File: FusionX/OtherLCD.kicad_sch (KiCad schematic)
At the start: 1 part, among them J3 OtherLCD

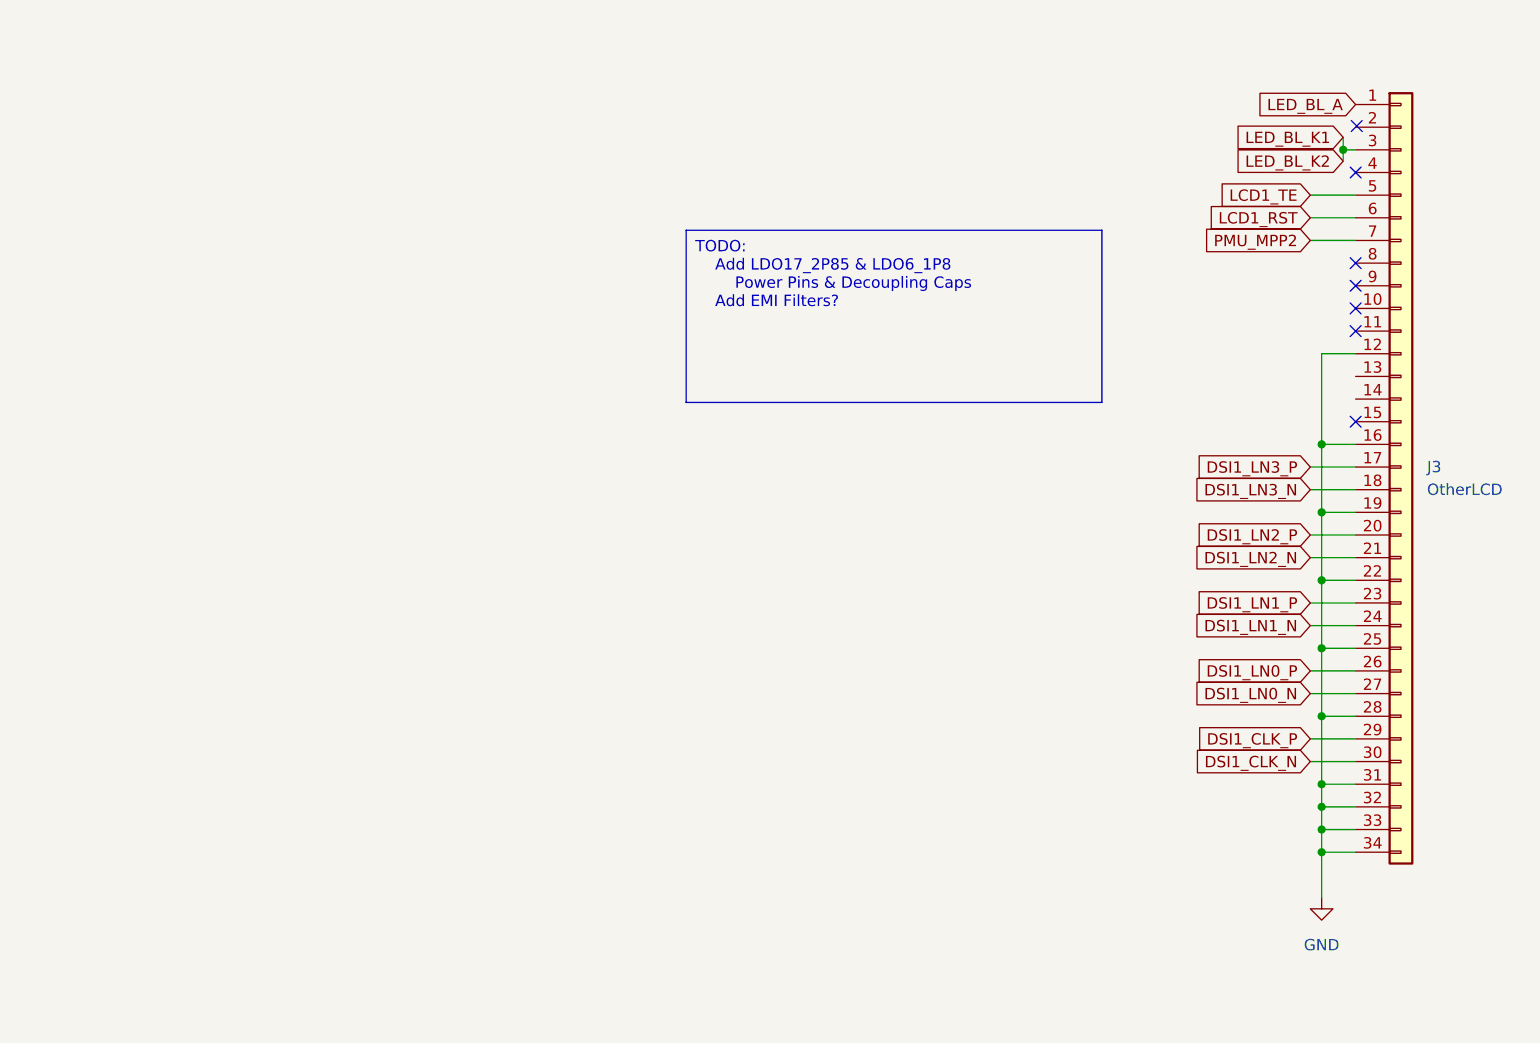
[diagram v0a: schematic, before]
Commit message: Implemented: 	USB-C Super Speed 	Capacitve Touch Screen 	Secondary LCD
Started On:
	PCB Layout
	Case Design
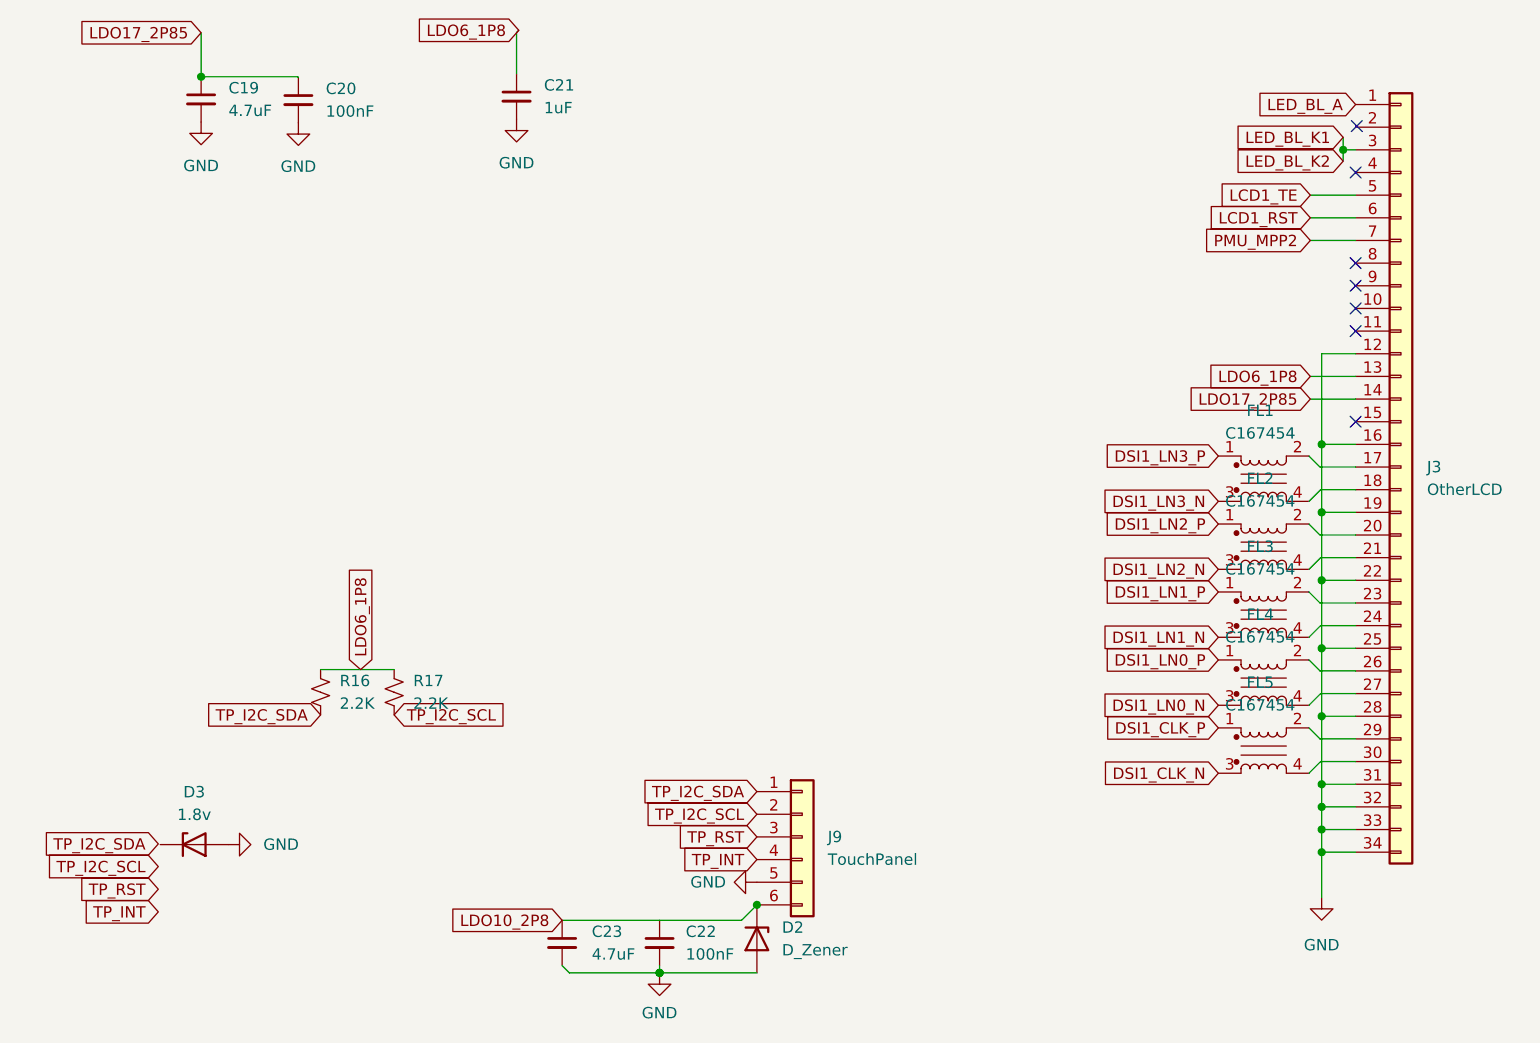
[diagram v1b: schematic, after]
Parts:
- added C19, C23: 4.7uF, symbol Device:C_Small
- added C20, C22: 100nF, symbol Device:C_Small
- added C21: 1uF, symbol Device:C_Small
- added D2: D_Zener, symbol Device:D_Zener
- added D3: 1.8v, symbol Device:D_Zener
- added FL1, FL2, FL3, FL4, FL5: C167454, Phone:DLP0SN900HL2L, symbol Device:Filter_EMI_CommonMode
- added J9: TouchPanel, symbol Connector_Generic:Conn_01x06
- added R16, R17: 2.2K, symbol Device:R_Small_US
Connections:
- net DSI1_CLK_N: now also FL5.3; no longer J3.30 (Pin_30)
- net DSI1_CLK_P: now also FL5.1; no longer J3.29 (Pin_29)
- net DSI1_LN0_N: now also FL4.3; no longer J3.27 (Pin_27)
- net DSI1_LN0_P: now also FL4.1; no longer J3.26 (Pin_26)
- net DSI1_LN1_N: now also FL3.3; no longer J3.24 (Pin_24)
- net DSI1_LN1_P: now also FL3.1; no longer J3.23 (Pin_23)
- net DSI1_LN2_N: now also FL2.3; no longer J3.21 (Pin_21)
- net DSI1_LN2_P: now also FL2.1; no longer J3.20 (Pin_20)
- net DSI1_LN3_N: now also FL1.3; no longer J3.18 (Pin_18)
- net DSI1_LN3_P: now also FL1.1; no longer J3.17 (Pin_17)
- net GND: now also C19.2, C20.2, C21.2, C22.2, C23.2, D2.2 (A), D3.2 (A), J9.5 (Pin_5)
- net LDO6_1P8: now reaches J3.13 (Pin_13)
- net LDO6_1P8: now also C21.1, R16.1, R17.1
- net LDO17_2P85: now reaches J3.14 (Pin_14)
- net LDO17_2P85: now also C19.1, C20.1
- new net: FL3.2, J3.23 (Pin_23)
- new net: FL3.4, J3.24 (Pin_24)
- new net: FL1.2, J3.17 (Pin_17)
- new net: FL1.4, J3.18 (Pin_18)
- new net: FL2.2, J3.20 (Pin_20)
- new net: FL2.4, J3.21 (Pin_21)
- new net: FL4.2, J3.26 (Pin_26)
- new net: FL4.4, J3.27 (Pin_27)
- new net: FL5.2, J3.29 (Pin_29)
- new net: FL5.4, J3.30 (Pin_30)
- new net LDO10_2P8: C23.1, D2.1 (K), J9.6 (Pin_6)
- new net TP_I2C_SCL: J9.2 (Pin_2), R17.2
- new net TP_I2C_SDA: J9.1 (Pin_1), R16.2
- new net TP_INT: J9.4 (Pin_4)
- new net TP_RST: J9.3 (Pin_3)
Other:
- company: (none) -> NoahGWood
- title: (none) -> FusionX

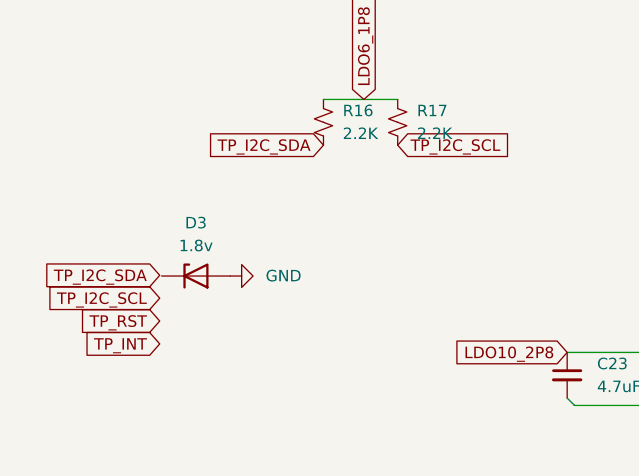
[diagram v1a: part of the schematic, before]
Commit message: Removed unneeded files
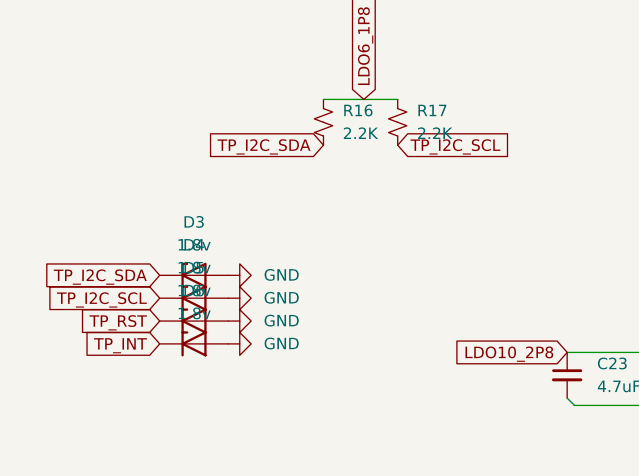
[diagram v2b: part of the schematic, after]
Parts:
- added D4, D5, D6: 1.8v, symbol Device:D_Zener
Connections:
- net GND: now also D4.2 (A), D5.2 (A), D6.2 (A)
- net TP_I2C_SCL: now also D4.1 (K)
- net TP_I2C_SDA: now also D3.1 (K)
- net TP_INT: now also D6.1 (K)
- net TP_RST: now also D5.1 (K)
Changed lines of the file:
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@@
+    )
+  )
+  (symbol (lib_id "Device:D_Zener") (at 40.5211 133.4371 0) (unit 1)
+    (in_bom yes) (on_board yes) (dnp no) (fields_autoplaced)
+    (property "Reference" "D4" (at 40.5211 127.5506 0)
+      (effects (font (size 1.27 1.27)))
+    )
+    (property "Value" "1.8v" (at 40.5211 130.0906 0)
+      (effects (font (size 1.27 1.27)))
+    )
+    (property "Footprint" "" (at 40.5211 133.4371 0)
+      (effects (font (size 1.27 1.27)) hide)
+    )
+    (property "Datasheet" "~" (at 40.5211 133.4371 0)
+      (effects (font (size 1.27 1.27)) hide)
+    )
+    (pin "1")
+    (pin "2")
+    (instances
+      (project "FusionX"
+        (path "/91d1c248-6dd5-47d7-a0ee-1ed6541bbbfb/cc596c66-0287-4740-9ece-2b1e4f18f9fd"
+          (reference "D4") (unit 1)
+        )
+      )
     )
   )
@@
     )
   )
-  (symbol (lib_id "Device:D_Zener") (at 40.7344 130.9745 0) (unit 1)
-    (in_bom yes) (on_board yes) (dnp no) (fields_autoplaced)
-    (property "Reference" "D3" (at 40.7344 125.088 0)
-      (effects (font (size 1.27 1.27)))
-    )
-    (property "Value" "1.8v" (at 40.7344 127.628 0)
-      (effects (font (size 1.27 1.27)))
-    )
-    (property "Footprint" "" (at 40.7344 130.9745 0)
-      (effects (font (size 1.27 1.27)) hide)
-    )
-    (property "Datasheet" "~" (at 40.7344 130.9745 0)
+  (symbol (lib_id "Device:D_Zener") (at 40.5211 138.5171 0) (unit 1)
+    (in_bom yes) (on_board yes) (dnp no) (fields_autoplaced)
+    (property "Reference" "D6" (at 40.5211 132.6306 0)
+      (effects (font (size 1.27 1.27)))
+    )
+    (property "Value" "1.8v" (at 40.5211 135.1706 0)
+      (effects (font (size 1.27 1.27)))
+    )
+    (property "Footprint" "" (at 40.5211 138.5171 0)
+      (effects (font (size 1.27 1.27)) hide)
+    )
+    (property "Datasheet" "~" (at 40.5211 138.5171 0)
+      (effects (font (size 1.27 1.27)) hide)
+    )
+    (pin "1")
+    (pin "2")
+    (instances
+      (project "FusionX"
+        (path "/91d1c248-6dd5-47d7-a0ee-1ed6541bbbfb/cc596c66-0287-4740-9ece-2b1e4f18f9fd"
+          (reference "D6") (unit 1)
+        )
+      )
+    )
+  )
+  (symbol (lib_id "Device:D_Zener") (at 40.5211 130.8971 0) (unit 1)
+    (in_bom yes) (on_board yes) (dnp no) (fields_autoplaced)
+    (property "Reference" "D3" (at 40.5211 125.0106 0)
+      (effects (font (size 1.27 1.27)))
+    )
+    (property "Value" "1.8v" (at 40.5211 127.5506 0)
+      (effects (font (size 1.27 1.27)))
+    )
+    (property "Footprint" "" (at 40.5211 130.8971 0)
+      (effects (font (size 1.27 1.27)) hide)
+    )
+    (property "Datasheet" "~" (at 40.5211 130.8971 0)
       (effects (font (size 1.27 1.27)) hide)
     )
@@
     )
   )
+  (symbol (lib_id "power:GND") (at 44.3311 135.9771 90) (unit 1)
+    (in_bom yes) (on_board yes) (dnp no) (fields_autoplaced)
+    (property "Reference" "#PWR078" (at 50.6811 135.9771 0)
+      (effects (font (size 1.27 1.27)) hide)
+    )
+    (property "Value" "GND" (at 48.2644 135.9771 90)
+      (effects (font (size 1.27 1.27)) (justify right))
+    )
+    (property "Footprint" "" (at 44.3311 135.9771 0)
+      (effects (font (size 1.27 1.27)) hide)
+    )
+    (property "Datasheet" "" (at 44.3311 135.9771 0)
+      (effects (font (size 1.27 1.27)) hide)
+    )
+    (pin "1")
+    (instances
+      (project "FusionX"
+        (path "/91d1c248-6dd5-47d7-a0ee-1ed6541bbbfb/cc596c66-0287-4740-9ece-2b1e4f18f9fd"
+          (reference "#PWR078") (unit 1)
+        )
+      )
+    )
+  )
   (symbol (lib_id "Device:R_Small_US") (at 54.9047 113.8943 0) (unit 1)
     (in_bom yes) (on_board yes) (dnp no) (fields_autoplaced)
@@
         (path "/91d1c248-6dd5-47d7-a0ee-1ed6541bbbfb/cc596c66-0287-4740-9ece-2b1e4f18f9fd"
           (reference "R16") (unit 1)
+        )
+      )
+    )
+  )
+  (symbol (lib_id "power:GND") (at 44.3311 133.4371 90) (unit 1)
+    (in_bom yes) (on_board yes) (dnp no) (fields_autoplaced)
+    (property "Reference" "#PWR05" (at 50.6811 133.4371 0)
+      (effects (font (size 1.27 1.27)) hide)
+    )
+    (property "Value" "GND" (at 48.2644 133.4371 90)
+      (effects (font (size 1.27 1.27)) (justify right))
+    )
+    (property "Footprint" "" (at 44.3311 133.4371 0)
+      (effects (font (size 1.27 1.27)) hide)
+    )
+    (property "Datasheet" "" (at 44.3311 133.4371 0)
+      (effects (font (size 1.27 1.27)) hide)
+    )
+    (pin "1")
+    (instances
+      (project "FusionX"
+        (path "/91d1c248-6dd5-47d7-a0ee-1ed6541bbbfb/cc596c66-0287-4740-9ece-2b1e4f18f9fd"
+          (reference "#PWR05") (unit 1)
         )
       )
@@
     )
   )
-  (symbol (lib_id "power:GND") (at 44.5444 130.9745 90) (unit 1)
-    (in_bom yes) (on_board yes) (dnp no) (fields_autoplaced)
-    (property "Reference" "#PWR077" (at 50.8944 130.9745 0)
-      (effects (font (size 1.27 1.27)) hide)
-    )
-    (property "Value" "GND" (at 48.4777 130.9745 90)
+  (symbol (lib_id "power:GND") (at 44.3311 130.8971 90) (unit 1)
+    (in_bom yes) (on_board yes) (dnp no) (fields_autoplaced)
+    (property "Reference" "#PWR077" (at 50.6811 130.8971 0)
+      (effects (font (size 1.27 1.27)) hide)
+    )
+    (property "Value" "GND" (at 48.2644 130.8971 90)
       (effects (font (size 1.27 1.27)) (justify right))
     )
-    (property "Footprint" "" (at 44.5444 130.9745 0)
-      (effects (font (size 1.27 1.27)) hide)
-    )
-    (property "Datasheet" "" (at 44.5444 130.9745 0)
+    (property "Footprint" "" (at 44.3311 130.8971 0)
+      (effects (font (size 1.27 1.27)) hide)
+    )
+    (property "Datasheet" "" (at 44.3311 130.8971 0)
       (effects (font (size 1.27 1.27)) hide)
     )
@@
     )
   )
+  (symbol (lib_id "Device:D_Zener") (at 40.5211 135.9771 0) (unit 1)
+    (in_bom yes) (on_board yes) (dnp no) (fields_autoplaced)
+    (property "Reference" "D5" (at 40.5211 130.0906 0)
+      (effects (font (size 1.27 1.27)))
+    )
+    (property "Value" "1.8v" (at 40.5211 132.6306 0)
+      (effects (font (size 1.27 1.27)))
+    )
+    (property "Footprint" "" (at 40.5211 135.9771 0)
+      (effects (font (size 1.27 1.27)) hide)
+    )
+    (property "Datasheet" "~" (at 40.5211 135.9771 0)
+      (effects (font (size 1.27 1.27)) hide)
+    )
+    (pin "1")
+    (pin "2")
+    (instances
+      (project "FusionX"
+        (path "/91d1c248-6dd5-47d7-a0ee-1ed6541bbbfb/cc596c66-0287-4740-9ece-2b1e4f18f9fd"
+          (reference "D5") (unit 1)
+        )
+      )
+    )
+  )
   (symbol (lib_id "Device:Filter_EMI_CommonMode") (at 160.6335 89.9546 0) (unit 1)
     (in_bom yes) (on_board yes) (dnp no) (fields_autoplaced)
@@
         )
       )
+    )
+  )
+  (symbol (lib_id "power:GND") (at 44.3311 138.5171 90) (unit 1)
+    (in_bom yes) (on_board yes) (dnp no) (fields_autoplaced)
+    (property "Reference" "#PWR079" (at 50.6811 138.5171 0)
+      (effects (font (size 1.27 1.27)) hide)
+    )
+    (property "Value" "GND" (at 48.2644 138.5171 90)
+      (effects (font (size 1.27 1.27)) (justify right))
+    )
+    (property "Footprint" "" (at 44.3311 138.5171 0)
+      (effects (font (size 1.27 1.27)) hide)
+    )
+    (property "Datasheet" "" (at 44.3311 138.5171 0)
+      (effects (font (size 1.27 1.27)) hide)
+    )
+    (pin "1")
+    (instances
+      (project "FusionX"
+        (path "/91d1c248-6dd5-47d7-a0ee-1ed6541bbbfb/cc596c66-0287-4740-9ece-2b1e4f18f9fd"
+          (reference "#PWR079") (unit 1)
+        )
+      )
